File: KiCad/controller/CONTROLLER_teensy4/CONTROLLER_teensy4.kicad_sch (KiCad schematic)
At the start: 7 parts, among them J3 jack2.5_PJ-210B, U1 Teensy4.0

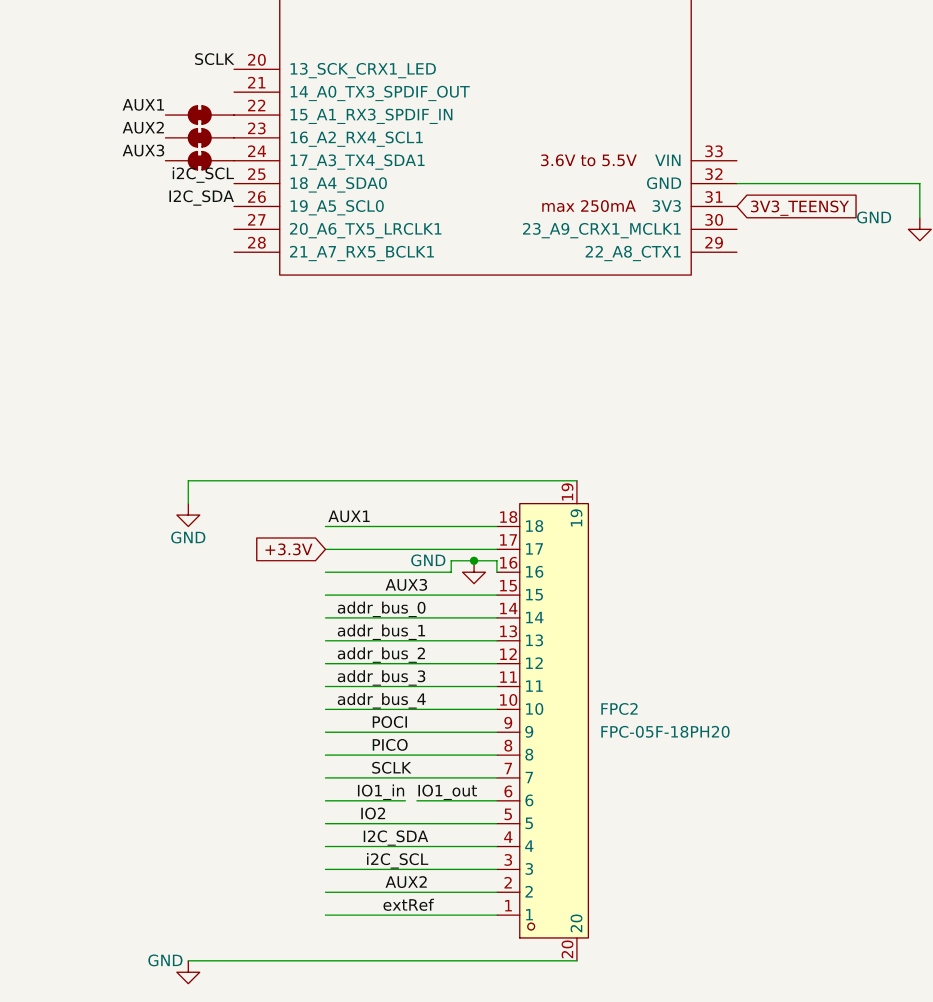
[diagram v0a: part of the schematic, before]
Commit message: major update: fixed inversion of i2c lines + added pull up resistors + rotated 180deg fpc conector
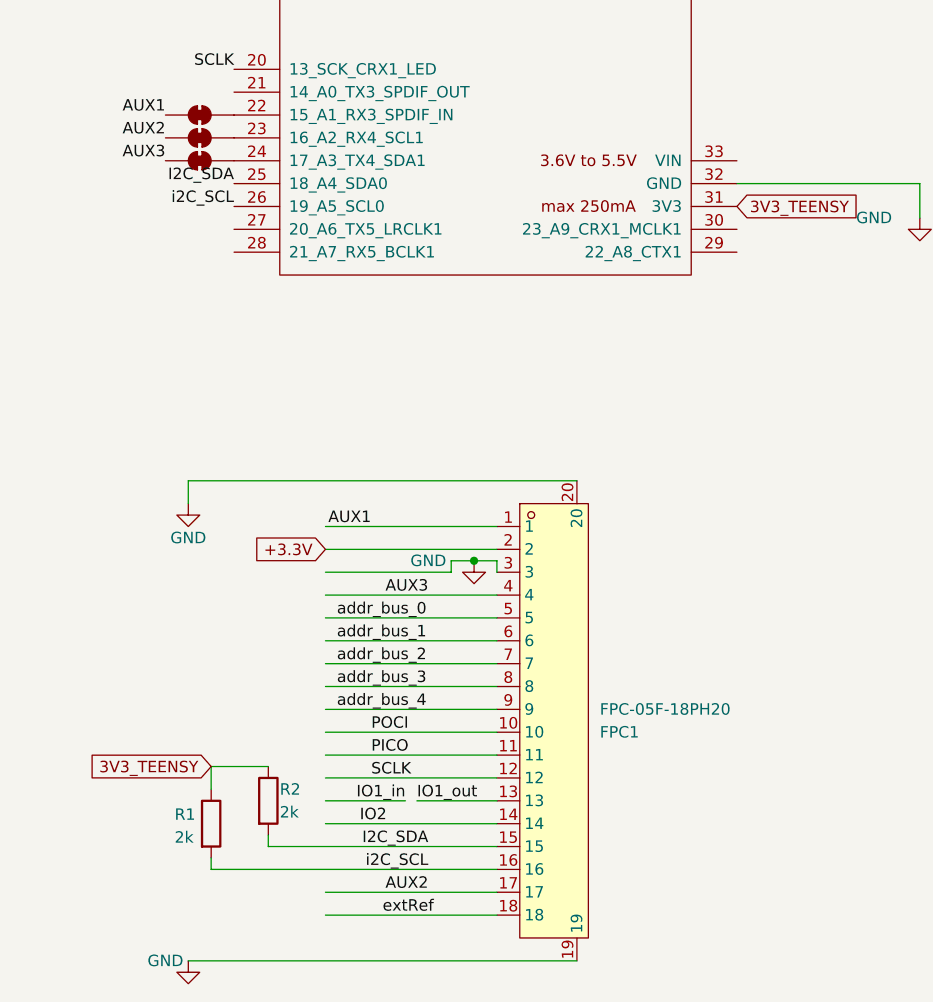
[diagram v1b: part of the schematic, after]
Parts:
- removed FPC2: FPC-05F-18PH20, 00_lcsc:FPC-SMD_18P-P0.50_X05C2018TZ, symbol 00_lcsc:FPC-05F-18PH20
- added FPC1: FPC-05F-18PH20, 00_lcsc:FPC-SMD_18P-P0.50_X05C2018TZ, symbol 00_lcsc:FPC-05F-18PH20
- added R1, R2: 2k, Resistor_SMD:R_0402_1005Metric_Pad0.72x0.64mm_HandSolder, symbol Device:R
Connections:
- net +3.3V: now also FPC1.2
- net 3V3_TEENSY: now also R1.1, R2.1
- net AUX1: now also FPC1.1
- net AUX2: now also FPC1.17
- net AUX3: now also FPC1.4
- net GND: now also FPC1.19, FPC1.20, FPC1.3
- net I2C_SDA: now also U1.25 (18_A4_SDA0), FPC1.15, R2.2; no longer U1.26 (19_A5_SCL0)
- net IO1_out: now also FPC1.13
- net IO2: now also FPC1.14
- net PICO: now also FPC1.11
- net POCI: now also FPC1.10
- net SCLK: now also FPC1.12
- net addr_bus_0: now also FPC1.5
- net addr_bus_1: now also FPC1.6
- net addr_bus_2: now also FPC1.7
- net addr_bus_3: now also FPC1.8
- net addr_bus_4: now also FPC1.9
- net extRef: now also FPC1.18
- net i2C_SCL: now also U1.26 (19_A5_SCL0), FPC1.16, R1.2; no longer U1.25 (18_A4_SDA0)

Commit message: fixed ref number of FPC connectors and added ref numbers of resitors
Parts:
- FPC1: LCSC Part C2856802 -> C397324
- R1, R2: LCSC Part (none) -> C4109
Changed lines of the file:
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@@
+			)
+		)
+		(property "LCSC Part" "C4109"
+			(at 48.26 170.18 0)
+			(effects
+				(font
+					(size 1.27 1.27)
+				)
+				(hide yes)
 			)
 		)
@@
 			)
 		)
-		(property "LCSC Part" "C2856802"
+		(property "LCSC Part" "C397324"
 			(at 85.09 195.58 0)
 			(effects
@@
 			(at 54.61 167.64 0)
 			(effects
+				(font
+					(size 1.27 1.27)
+				)
+				(hide yes)
+			)
+		)
+		(property "LCSC Part" "C4109"
+			(at 54.61 167.64 0)
+			(effects

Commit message: minor fix on teensy shield
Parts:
- removed JP4: SolderJumper_3_Bridged12, Jumper:SolderJumper-3_P1.3mm_Bridged12_Pad1.0x1.5mm, symbol Jumper:SolderJumper_3_Bridged12
- added J2: Conn_01x02_Pin, Connector_PinHeader_1.27mm:PinHeader_1x02_P1.27mm_Vertical, symbol Connector:Conn_01x02_Pin
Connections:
- net 3V3_TEENSY is gone; now on net +3.3V: R1.1, R2.1, U1.31 (3V3)
- net GND: now also J2.2 (Pin_2)
- net VSYS: now reaches U1.33 (VIN)
- net VSYS: now also J2.1 (Pin_1)
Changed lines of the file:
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@@
 		)
 	)
-	(global_label "3V3_BAT"
+	(global_label "+3.3V"
 		(shape input)
-		(at 135.89 57.15 270)
+		(at 106.68 101.6 0)
 		(fields_autoplaced yes)
 		(effects
@@
 				(size 1.27 1.27)
 			)
-			(justify right)
+			(justify left)
 		)
 		(property "Intersheetrefs" "${INTERSHEET_REFS}"
-			(at 135.89 67.9366 90)
-			(effects
-				(font
-					(size 1.27 1.27)
-				)
-				(justify right)
-				(hide yes)
-			)
-		)
-	)
-	(global_label "3V3_TEENSY"
+			(at 115.35 101.6 0)
+			(effects
+				(font
+					(size 1.27 1.27)
+				)
+				(justify left)
+				(hide yes)
+			)
+		)
+	)
+	(global_label "VSYS"
 		(shape input)
-		(at 125.73 57.15 270)
+		(at 106.68 96.52 0)
 		(fields_autoplaced yes)
 		(effects
@@
 				(size 1.27 1.27)
 			)
-			(justify right)
+			(justify left)
 		)
 		(property "Intersheetrefs" "${INTERSHEET_REFS}"
-			(at 125.73 71.5046 90)
-			(effects
-				(font
-					(size 1.27 1.27)
-				)
-				(justify right)
-				(hide yes)
-			)
-		)
-	)
-	(global_label "3V3_TEENSY"
+			(at 114.2614 96.52 0)
+			(effects
+				(font
+					(size 1.27 1.27)
+				)
+				(justify left)
+				(hide yes)
+			)
+		)
+	)
+	(global_label "GND"
 		(shape input)
-		(at 48.26 163.83 180)
+		(at 195.58 50.8 0)
 		(fields_autoplaced yes)
 		(effects
@@
 				(size 1.27 1.27)
 			)
-			(justify right)
+			(justify left)
 		)
 		(property "Intersheetrefs" "${INTERSHEET_REFS}"
-			(at 33.9054 163.83 0)
-			(effects
-				(font
-					(size 1.27 1.27)
-				)
-				(justify right)
+			(at 202.3563 50.8 0)
+			(effects
+				(font
+					(size 1.27 1.27)
+				)
+				(justify left)
 				(hide yes)
 			)
@@
 	(global_label "+3.3V"
 		(shape input)
-		(at 130.81 60.96 270)
+		(at 48.26 163.83 180)
 		(fields_autoplaced yes)
 		(effects
@@
 		)
 		(property "Intersheetrefs" "${INTERSHEET_REFS}"
-			(at 130.81 69.63 90)
+			(at 39.59 163.83 0)
 			(effects
 				(font
@@
 		)
 	)
-	(global_label "3V3_TEENSY"
+	(global_label "VSYS"
 		(shape input)
-		(at 106.68 101.6 0)
+		(at 195.58 48.26 0)
 		(fields_autoplaced yes)
 		(effects
@@
 		)
 		(property "Intersheetrefs" "${INTERSHEET_REFS}"
-			(at 120.9552 101.6 0)
+			(at 203.1614 48.26 0)
 			(effects
 				(font
@@
 	)
 	(symbol
+		(lib_id "Connector:Conn_01x02_Pin")
+		(at 190.5 48.26 0)
+		(unit 1)
+		(exclude_from_sim no)
+		(in_bom yes)
+		(on_board yes)
+		(dnp no)
+		(fields_autoplaced yes)
+		(property "Reference" "J2"
+			(at 191.135 43.18 0)
+			(effects
+				(font
+					(size 1.27 1.27)
+				)
+			)
+		)
+		(property "Value" "Conn_01x02_Pin"
+			(at 191.135 45.72 0)
+			(effects
+				(font
+					(size 1.27 1.27)
+				)
+			)
+		)
+		(property "Footprint" "Connector_PinHeader_1.27mm:PinHeader_1x02_P1.27mm_Vertical"
+			(at 190.5 48.26 0)
+			(effects
+				(font
+					(size 1.27 1.27)
+				)
+				(hide yes)
+			)
+		)
+		(property "Datasheet" "~"
+			(at 190.5 48.26 0)
+			(effects
+				(font
+					(size 1.27 1.27)
+				)
+				(hide yes)
+			)
+		)
+		(property "Description" "Generic connector, single row, 01x02, script generated"
+			(at 190.5 48.26 0)
+			(effects
+				(font
+					(size 1.27 1.27)
+				)
+				(hide yes)
+			)
+		)
+		(pin "1"
+		)
+		(pin "2"
+		)
+		(instances
+			(project "CONTROLLER_teensy4"
+				(path "/96967913-6ef1-489a-a725-ff0b6a23f183"
+					(reference "J2")
+					(unit 1)
+				)
+			)
+		)
+	)
+	(symbol
 		(lib_id "Jumper:SolderJumper_2_Bridged")
 		(at 46.99 91.44 0)
@@
 					(unit 1)
 				)
-			)
-		)
-	)
-	(symbol
-		(lib_id "Jumper:SolderJumper_3_Bridged12")
-		(at 130.81 57.15 0)
-		(unit 1)
-		(exclude_from_sim yes)
-		(in_bom no)
-		(on_board yes)
-		(dnp no)
-		(fields_autoplaced yes)
-		(property "Reference" "JP4"
-			(at 130.81 50.8 0)
-			(effects
-				(font
-					(size 1.27 1.27)
-				)
-			)
-		)
-		(property "Value" "SolderJumper_3_Bridged12"
-			(at 130.81 53.34 0)
-			(effects
-				(font
-					(size 1.27 1.27)
-				)
-			)
-		)
-		(property "Footprint" "Jumper:SolderJumper-3_P1.3mm_Bridged12_Pad1.0x1.5mm"
-			(at 130.81 57.15 0)
-			(effects
-				(font
-					(size 1.27 1.27)
-				)
-				(hide yes)
-			)
-		)
-		(property "Datasheet" "~"
-			(at 130.81 57.15 0)
-			(effects
-				(font
-					(size 1.27 1.27)
-				)
-				(hide yes)
-			)
-		)
-		(property "Description" "3-pole Solder Jumper, pins 1+2 closed/bridged"
-			(at 130.81 57.15 0)
-			(effects
-				(font
-					(size 1.27 1.27)
-				)
-				(hide yes)
-			)
-		)
-		(pin "3"
-		)
-		(pin "1"
-		)
-		(pin "2"
-		)
-		(instances
-			(project "CONTROLLER_teensy4"
-				(path "/96967913-6ef1-489a-a725-ff0b6a23f183"
-					(reference "JP4")
-					(unit 1)
-				)
